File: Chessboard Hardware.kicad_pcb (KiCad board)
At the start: 2 copper layers, 199 x 199 mm, 92 parts, among them J1 Conn_01x04_Pin

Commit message: Layout mounting holes, update SS49E footprint to be smaller
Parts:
- moved H1 357.4 mm to (54.0, 54.0)
- moved H4 338.4 mm to (54.0, 245.0)
- moved H2 194.8 mm to (245.0, 54.0)
- moved H3 153.7 mm to (245.0, 245.0)

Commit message: Oops forgot decoupling caps
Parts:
- added C1: 100nF, Capacitor_THT:C_Disc_D5.0mm_W2.5mm_P2.50mm, B.Cu at (140.2, 54.0)
- added C2: 100nF, Capacitor_THT:C_Disc_D5.0mm_W2.5mm_P2.50mm, B.Cu at (140.2, 78.5)
- added C3: 100nF, Capacitor_THT:C_Disc_D5.0mm_W2.5mm_P2.50mm, B.Cu at (140.2, 103.5)
- added C4: 100nF, Capacitor_THT:C_Disc_D5.0mm_W2.5mm_P2.50mm, B.Cu at (140.2, 128.5)
- added C5: 100nF, Capacitor_THT:C_Disc_D5.0mm_W2.5mm_P2.50mm, B.Cu at (140.2, 154.0)
- added C6: 100nF, Capacitor_THT:C_Disc_D5.0mm_W2.5mm_P2.50mm, B.Cu at (140.2, 179.0)
- added C7: 100nF, Capacitor_THT:C_Disc_D5.0mm_W2.5mm_P2.50mm, B.Cu at (140.2, 204.0)
- added C8: 100nF, Capacitor_THT:C_Disc_D5.0mm_W2.5mm_P2.50mm, B.Cu at (140.2, 229.0)

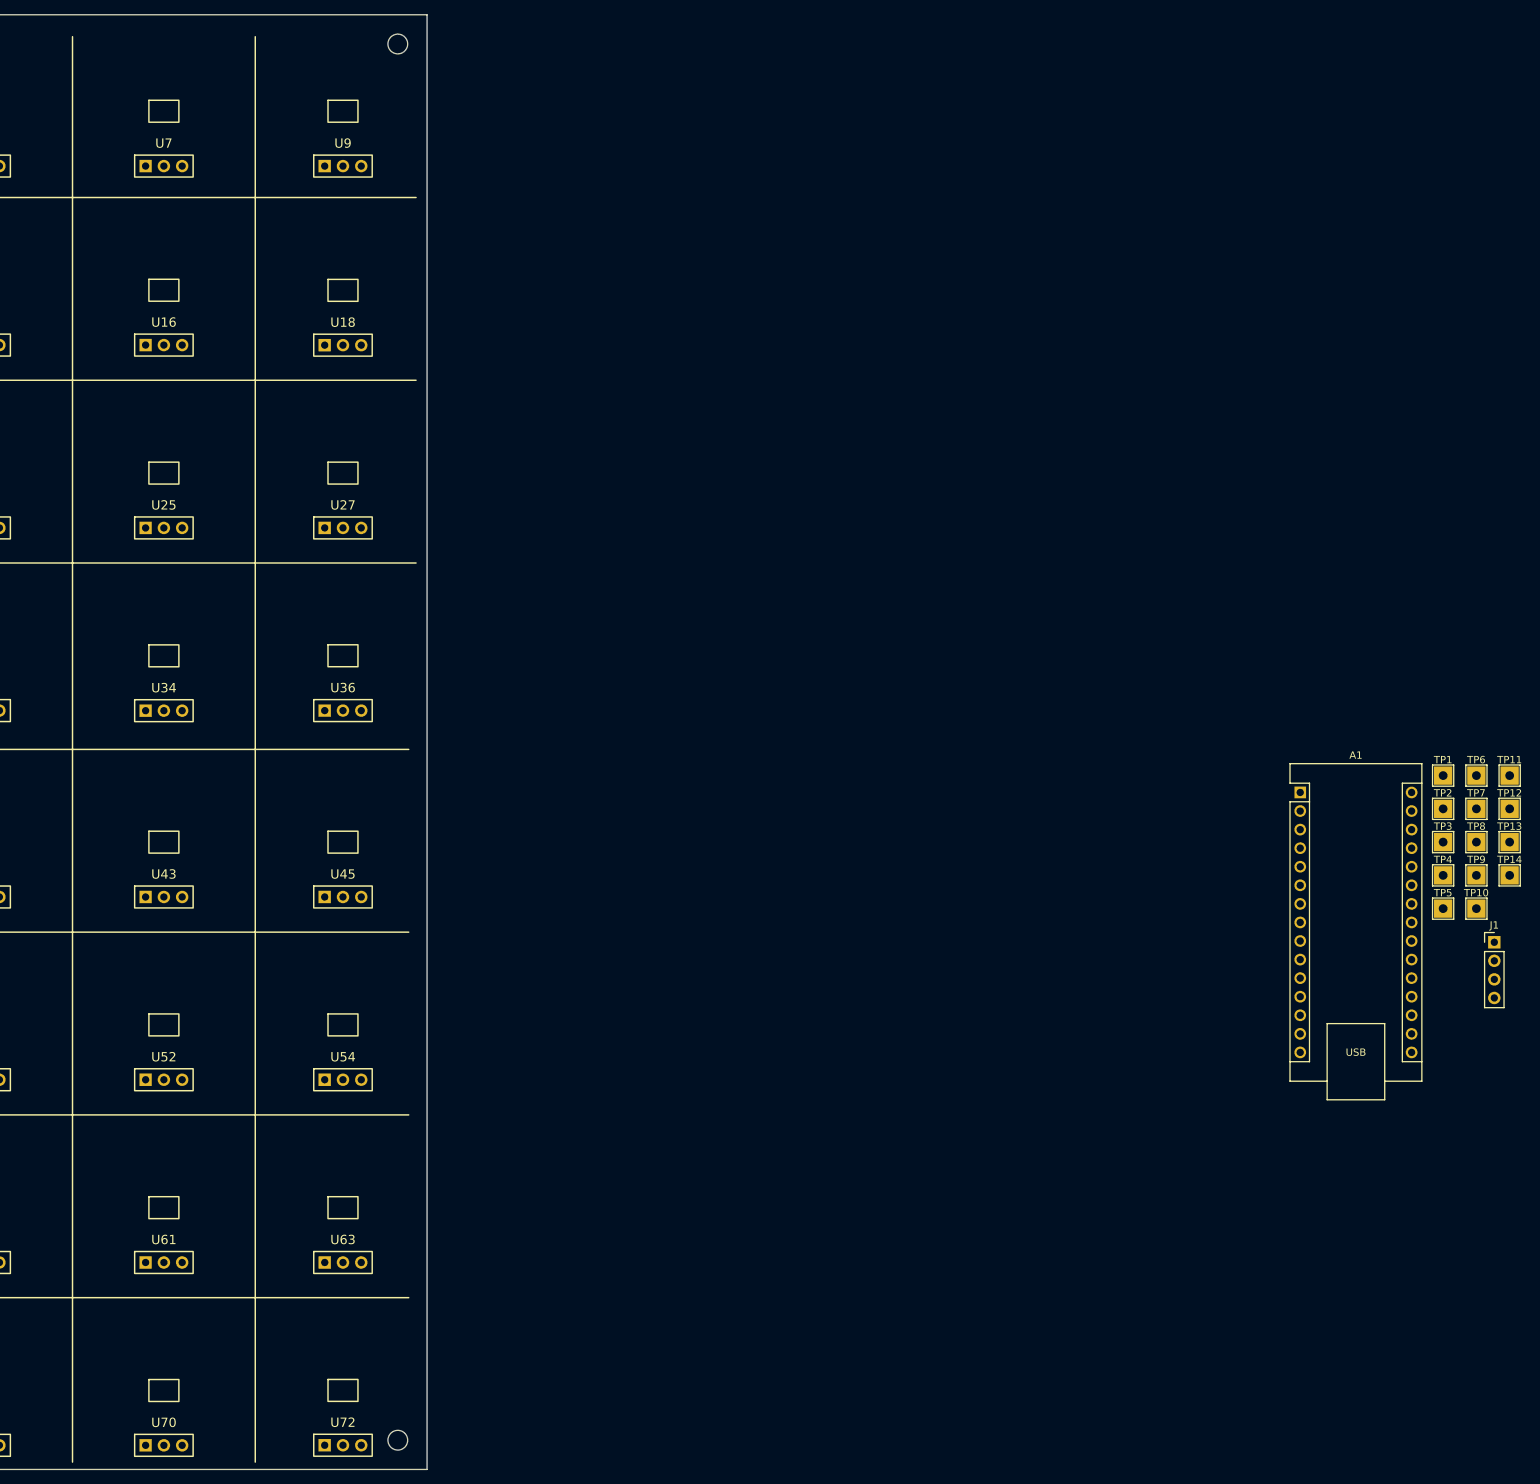
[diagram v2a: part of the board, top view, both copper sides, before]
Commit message: Finish placing except test points, which have 2.54 pin header footprint now
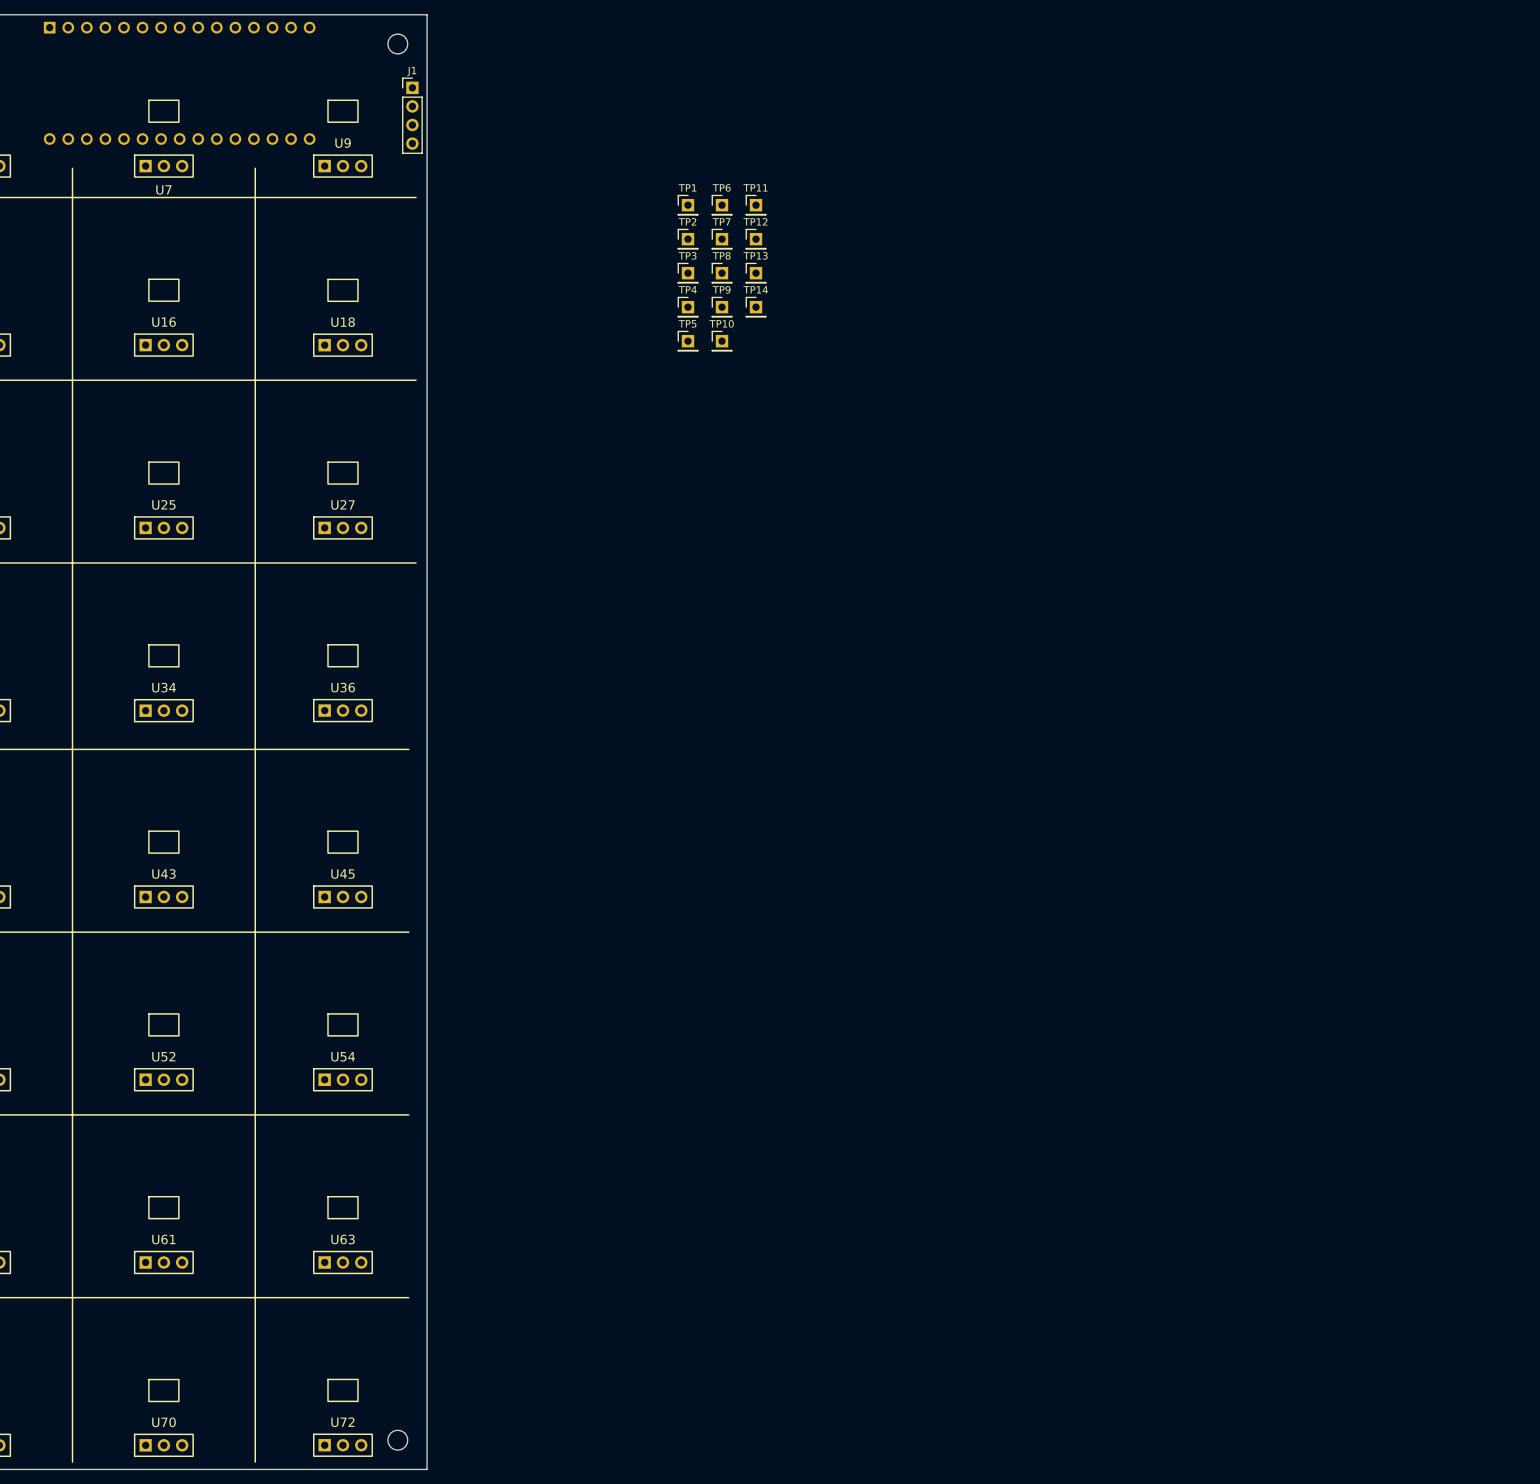
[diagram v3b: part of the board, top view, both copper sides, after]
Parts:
- A1: moved to B.Cu
- TP1, TP10, TP11, TP12, TP13, TP14, TP2, TP3, TP4, TP5, TP6, TP7, TP8, TP9: footprint TestPoint:TestPoint_THTPad_2.5x2.5mm_Drill1.2mm -> Connector_PinHeader_2.54mm:PinHeader_1x01_P2.54mm_Vertical
- moved A1 200.5 mm to (197.4, 51.8), turned to -90 degrees
- moved J1 188.6 mm to (247.0, 60.0)
- moved TP1 129.5 mm to (284.7, 76.0)
- moved TP2 129.4 mm to (284.7, 80.7)
- moved TP6 129.4 mm to (289.4, 76.0)
- moved TP3 129.3 mm to (284.7, 85.3)
- moved TP7 129.3 mm to (289.4, 80.7)
- moved TP11 129.3 mm to (294.0, 76.0)
- moved TP4 129.3 mm to (284.7, 90.0)
- moved TP8 129.3 mm to (289.4, 85.3)
- moved TP12 129.2 mm to (294.0, 80.7)
- moved TP5 129.2 mm to (284.7, 94.7)
- moved TP9 129.2 mm to (289.4, 90.0)
- moved TP13 129.2 mm to (294.0, 85.3)
- moved TP10 129.1 mm to (289.4, 94.7)
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
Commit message: Start routing
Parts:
- removed TP1, TP10, TP11, TP12, TP13, TP14, TP2, TP3, TP4, TP5, TP6, TP7, TP8, TP9: TestPoint, Connector_PinHeader_2.54mm:PinHeader_1x01_P2.54mm_Vertical
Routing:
- net GND: track 0.00 -> 1850.0 mm, vias 0 -> 1
- net VCC: track 0.00 -> 1796.1 mm
- net /INH: track 0.00 -> 212.8 mm
- net /A: track 0.00 -> 201.2 mm, vias 0 -> 7
- net /B: track 0.00 -> 195.4 mm, vias 0 -> 7
- net /C: track 0.00 -> 189.1 mm
- net /TX: track 0.00 -> 58.3 mm
- net /RX: track 0.00 -> 55.5 mm

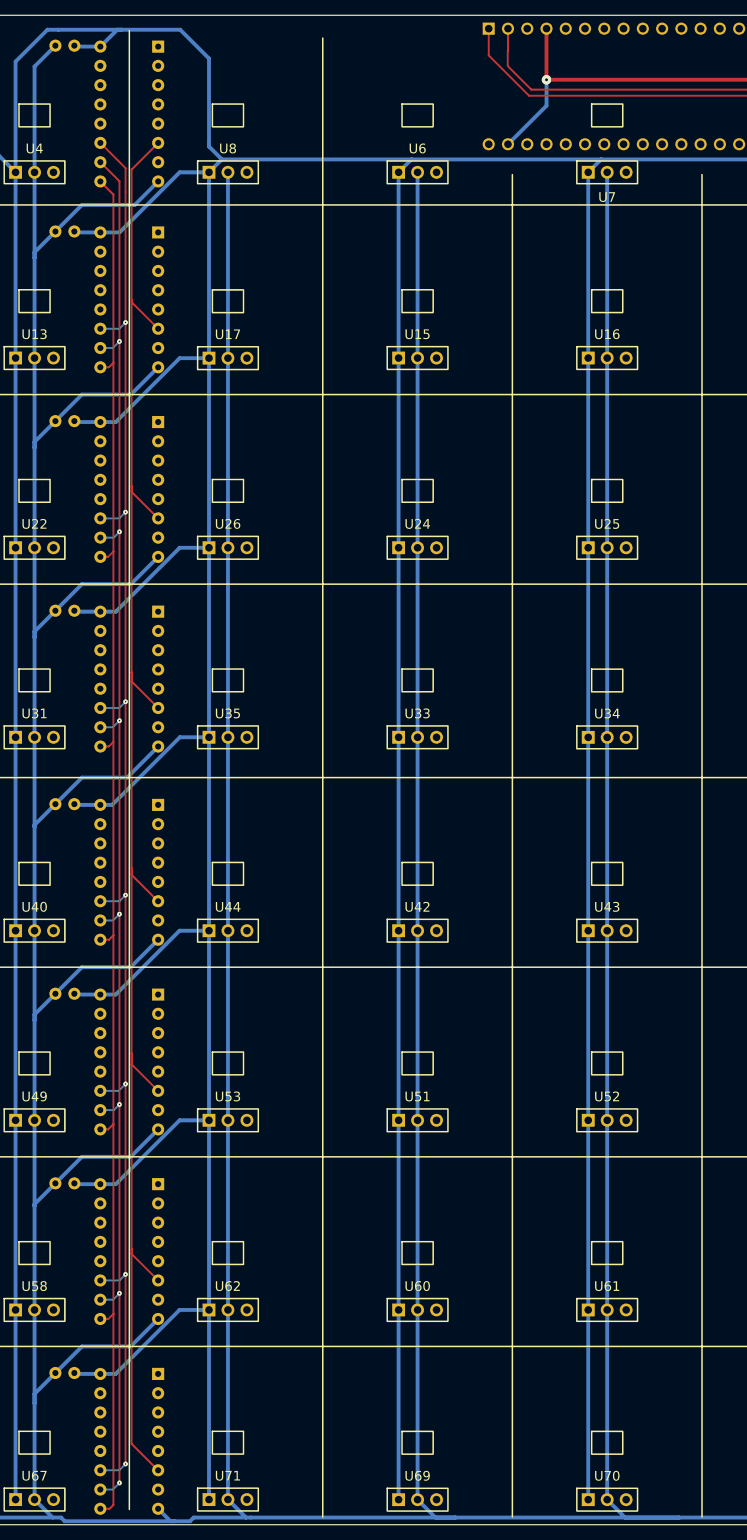
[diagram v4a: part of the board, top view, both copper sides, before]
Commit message: Done routing everything except linear halls
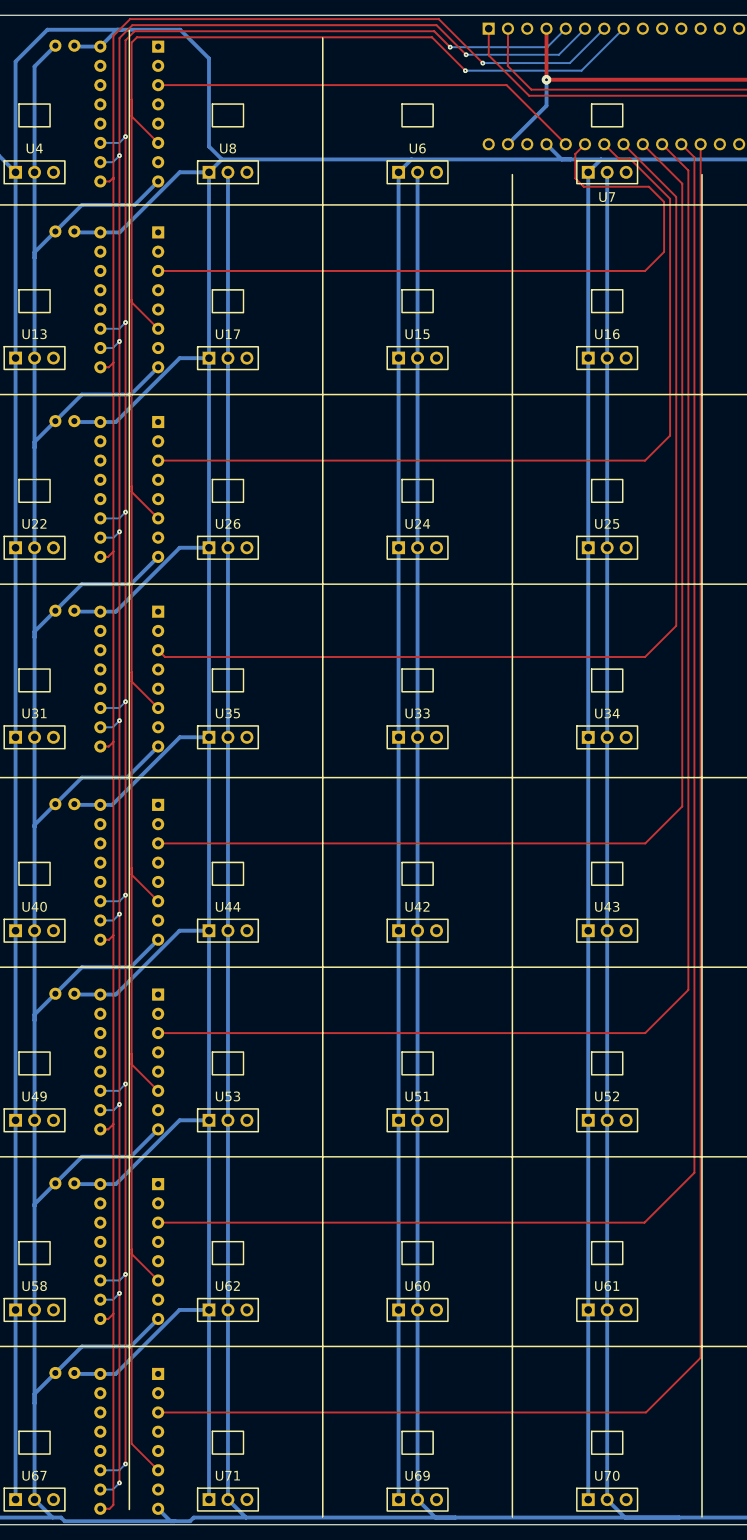
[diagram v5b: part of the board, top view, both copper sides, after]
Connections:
- A1 pad 19: /COM0 -> /COM7
- A1 pad 20: /COM1 -> /COM6
- A1 pad 21: /COM2 -> /COM5
- A1 pad 22: /COM3 -> /COM4
- A1 pad 23: /COM4 -> /COM3
- A1 pad 24: /COM5 -> /COM2
- A1 pad 25: /COM6 -> /COM1
- A1 pad 26: /COM7 -> /COM0
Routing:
- net /COM7: track 0.00 -> 234.5 mm
- net /COM6: track 0.00 -> 209.7 mm
- net /COM5: track 0.00 -> 185.2 mm
- net /COM4: track 0.00 -> 160.6 mm
- net /COM3: track 0.00 -> 136.7 mm
- net /COM2: track 0.00 -> 111.7 mm
- net /COM1: track 0.00 -> 92.4 mm
- net /C: track 189.1 -> 279.6 mm, vias 0 -> 1
- net /INH: track 212.8 -> 301.0 mm, vias 0 -> 1
- net /B: track 195.4 -> 278.6 mm, vias 7 -> 9
- net /A: track 201.2 -> 277.4 mm, vias 7 -> 9
- net /COM0: track 0.00 -> 57.0 mm
- net VCC: track 1796.1 -> 1799.9 mm
